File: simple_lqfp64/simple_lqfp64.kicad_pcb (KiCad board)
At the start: 2 copper layers, 47 parts, among them P1 CONN_01X02, P10 CONN_01X04, P11 CONN_01X03, P12 CONN_01X03, P13 USB_A, P14 CONN_01X01, P15 CONN_01X01, P16 CONN_01X01, P17 CONN_01X01, P18 CONN_01X01, P19 CONN_01X01, P2 CONN_01X03, P20 CONN_01X01, P21 CONN_01X01, P22 CONN_01X01, P23 CONN_01X01, P24 CONN_01X01, P25 CONN_01X01, P26 CONN_01X01, P27 CONN_01X01, P28 CONN_01X01, P29 CONN_01X01, P3 CONN_01X04, P30 CONN_01X01, P31 CONN_01X01, P32 CONN_01X01, P33 CONN_01X01, P4 CONN_01X04, P5 CONN_01X01, P6 CONN_01X04, P7 CONN_01X03, P8 CONN_01X06, P9 CONN_01X07, SW1 SW_PUSH, U1 STM32F103RCTx, U2 AP1117D33, Y1 Crystal, Y2 Crystal

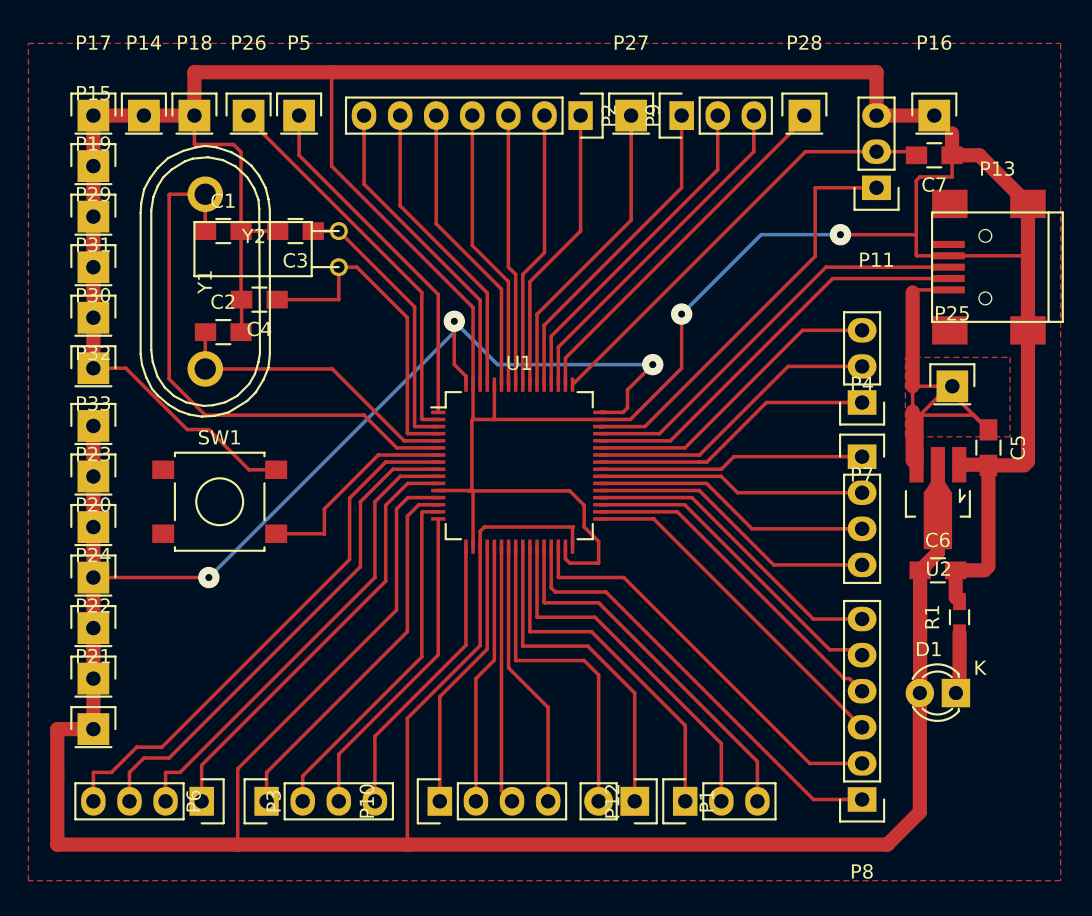
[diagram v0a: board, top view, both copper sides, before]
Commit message: stm32 lqfp64 fixes
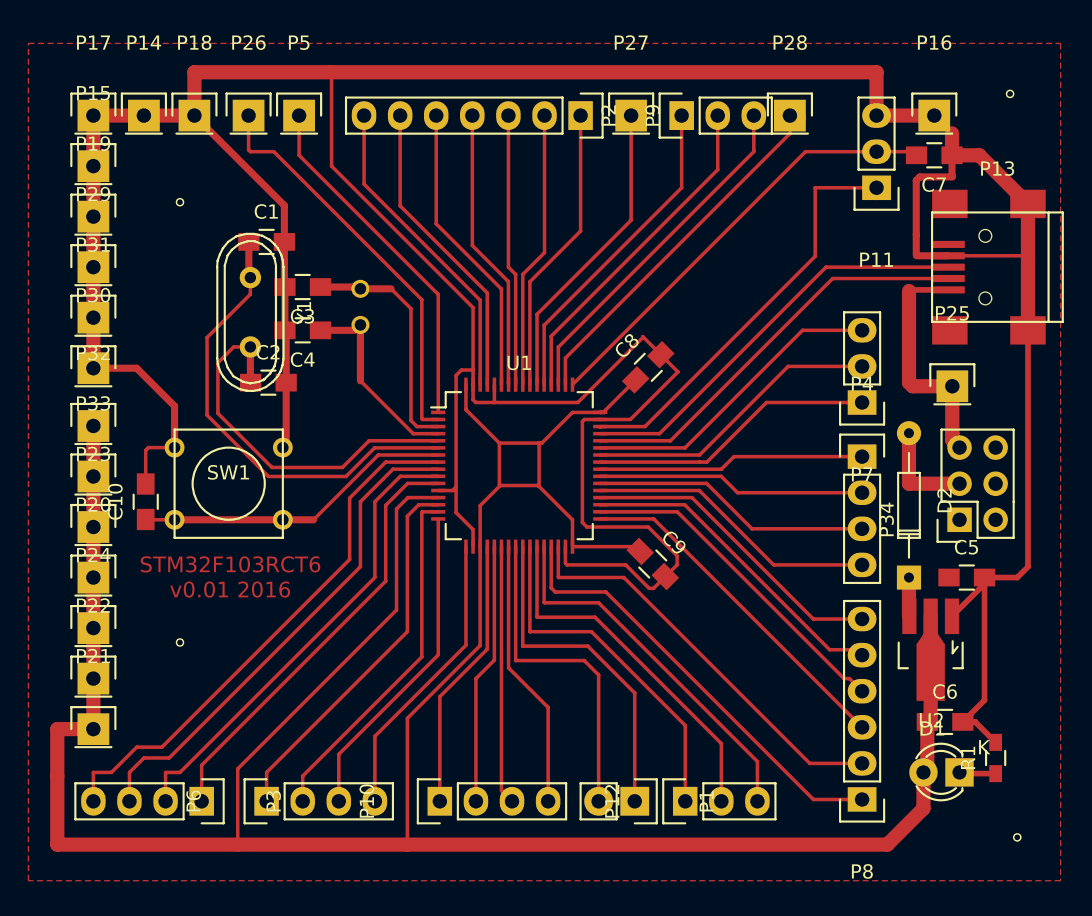
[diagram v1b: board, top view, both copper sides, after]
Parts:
- added C10: 100nF, Capacitors_SMD:C_0805_HandSoldering, F.Cu at (128.7, 77.5)
- added C8: 100nF, Capacitors_SMD:C_0805_HandSoldering, F.Cu at (164.0, 68.0)
- added C9: 100nF, Capacitors_SMD:C_0805_HandSoldering, F.Cu at (164.3, 81.9)
- added D2: D, Diodes_ThroughHole:Diode_DO-35_SOD27_Horizontal_RM10, F.Cu at (182.4, 82.8)
- added P34: CONN_02X03, Socket_Strips:Socket_Strip_Straight_2x03, F.Cu at (185.9, 78.7)
- SW1: footprint Buttons_Switches_SMD:SW_SPST_B3S-1000 -> Buttons_Switches_ThroughHole:SW_PUSH_SMALL
- Y1: footprint Crystals:Crystal_HC48-U_Vertical -> Crystals:Crystal_HC49-U_Vertical
- Y2: moved to B.Cu
- moved U2 10.7 mm to (183.9, 87.9)
- moved C6 10.7 mm to (184.9, 93.0)
- moved R1 10.2 mm to (188.5, 95.5)
- moved C5 9.27 mm to (186.4, 82.8), turned to 0 degrees
- moved D1 5.59 mm to (185.9, 96.5)
- moved C2 4.77 mm to (137.3, 69.1)
- moved Y2 4.34 mm to (143.8, 63.8)
- moved C3 3.97 mm to (139.7, 62.4)
- moved Y1 3.84 mm to (136.0, 64.1)
- moved C4 3.74 mm to (139.7, 65.4)
- moved C1 3.14 mm to (137.2, 59.2)
- moved SW1 1.42 mm to (134.5, 76.2)
- moved P28 1.02 mm to (174.0, 50.3)
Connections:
- C5 pad 1: +5V -> Net-(C5-Pad1)
- P13 pad 1: +5V -> Net-(P13-Pad1)
- P25 pad 1: +5V -> Net-(P13-Pad1)
- U2 pad 3: +5V -> Net-(C5-Pad1)
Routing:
- net +3V3: track 244.3 -> 207.0 mm, vias 3 -> 0
- net +5V: track 34.5 -> 7.11 mm
- net Net-(P13-Pad1): track 0.00 -> 17.7 mm
- net GND: track 279.8 -> 292.8 mm, vias 2 -> 0
- net Net-(C4-Pad1): track 23.2 -> 13.9 mm
- net Net-(C10-Pad1): track 14.8 -> 22.5 mm
- net Net-(C1-Pad1): track 39.1 -> 32.4 mm
- net Net-(C2-Pad1): track 21.1 -> 26.8 mm
- net Net-(C5-Pad1): track 0.00 -> 2.74 mm
- net Net-(C3-Pad1): track 19.4 -> 17.0 mm
- net Net-(D1-Pad1): track 4.34 -> 2.57 mm
- net Net-(P26-Pad1): track 27.6 -> 28.8 mm
- net (no net): vias 0 -> 4
- removed copper zone on F.Cu, net +5V
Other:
- board text added: "STM32F103RCT6 v0.01 2016"
